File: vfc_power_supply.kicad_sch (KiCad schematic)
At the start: 27 parts, among them J1 Conn_01x03_Male, J2 Raspberry_Pi_4B, J3 Conn_01x02_Male, J4 Conn_01x06_Female, M1 Logo_10mmx10mm

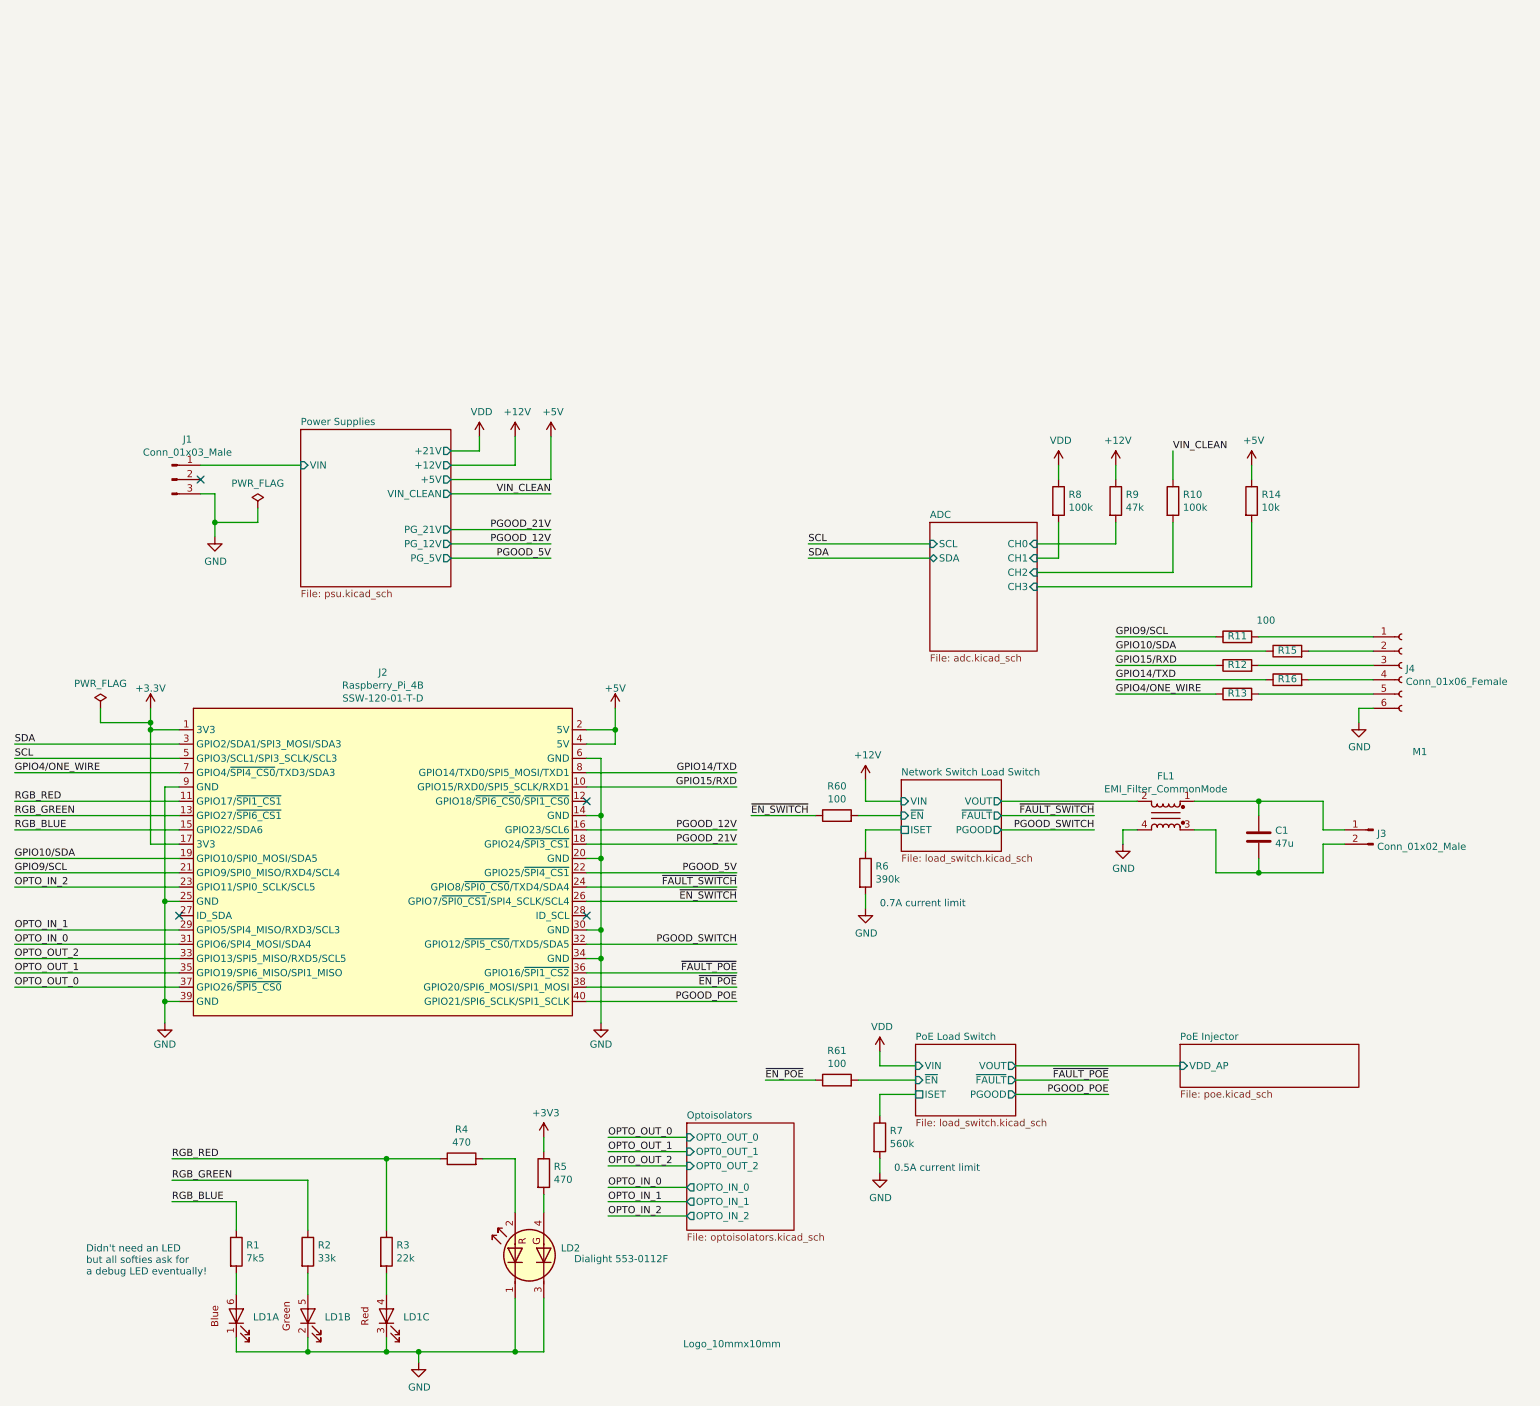
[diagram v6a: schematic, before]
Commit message: Tweaked component values to working. Added rear panel PCB
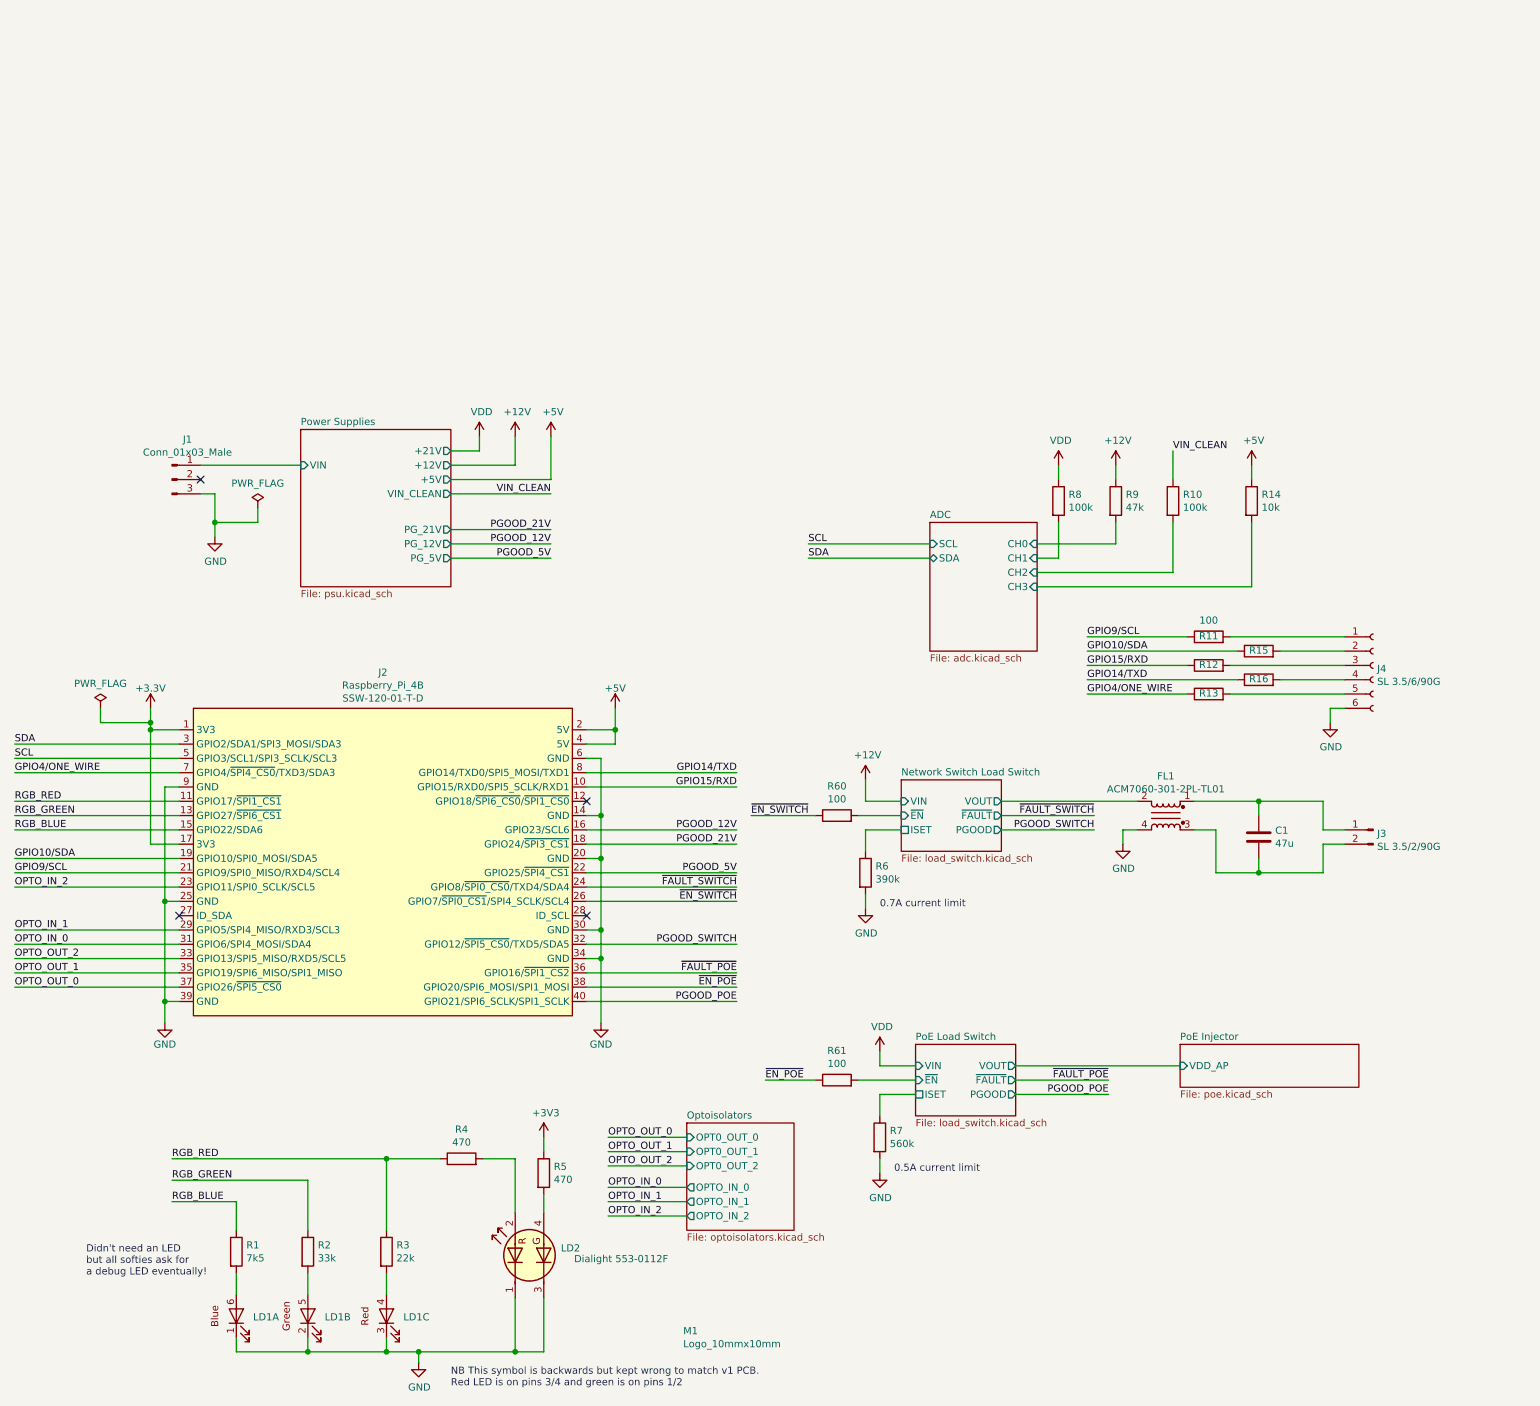
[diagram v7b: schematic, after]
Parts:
- FL1: value EMI_Filter_CommonMode -> ACM7060-301-2PL-TL01
- J3: value Conn_01x02_Male -> SL 3.5/2/90G
- J4: value Conn_01x06_Female -> SL 3.5/6/90G
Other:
- note added: "NB This symbol is backwards but kept wrong to match v1 PCB. Red LED is on pins 3/4 and green is on pins 1/2"
- moved on the sheet: J4, R11, R12, R13, R15, R16
